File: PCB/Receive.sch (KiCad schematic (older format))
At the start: 36 parts, among them U18 MAX5394L, U19 MAX5394L, U20 MAX11116, U21 TLV3544, U22 MCP6L1

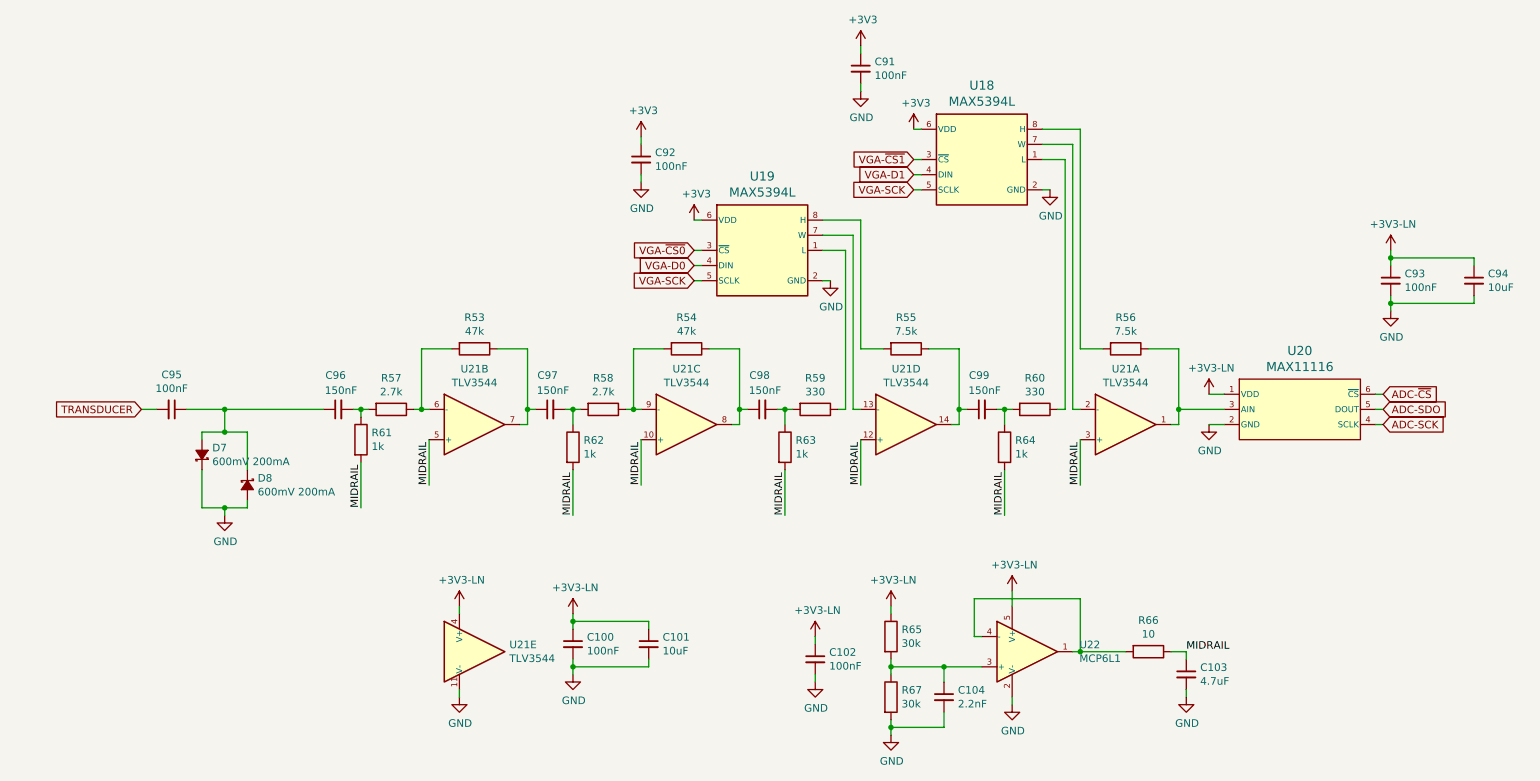
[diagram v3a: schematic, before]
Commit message: Remove unnecessary series resistors, rearrange connections on FPGA and microcontroller, rearrange debug pins, layout most of FPGA and microcontroller sections
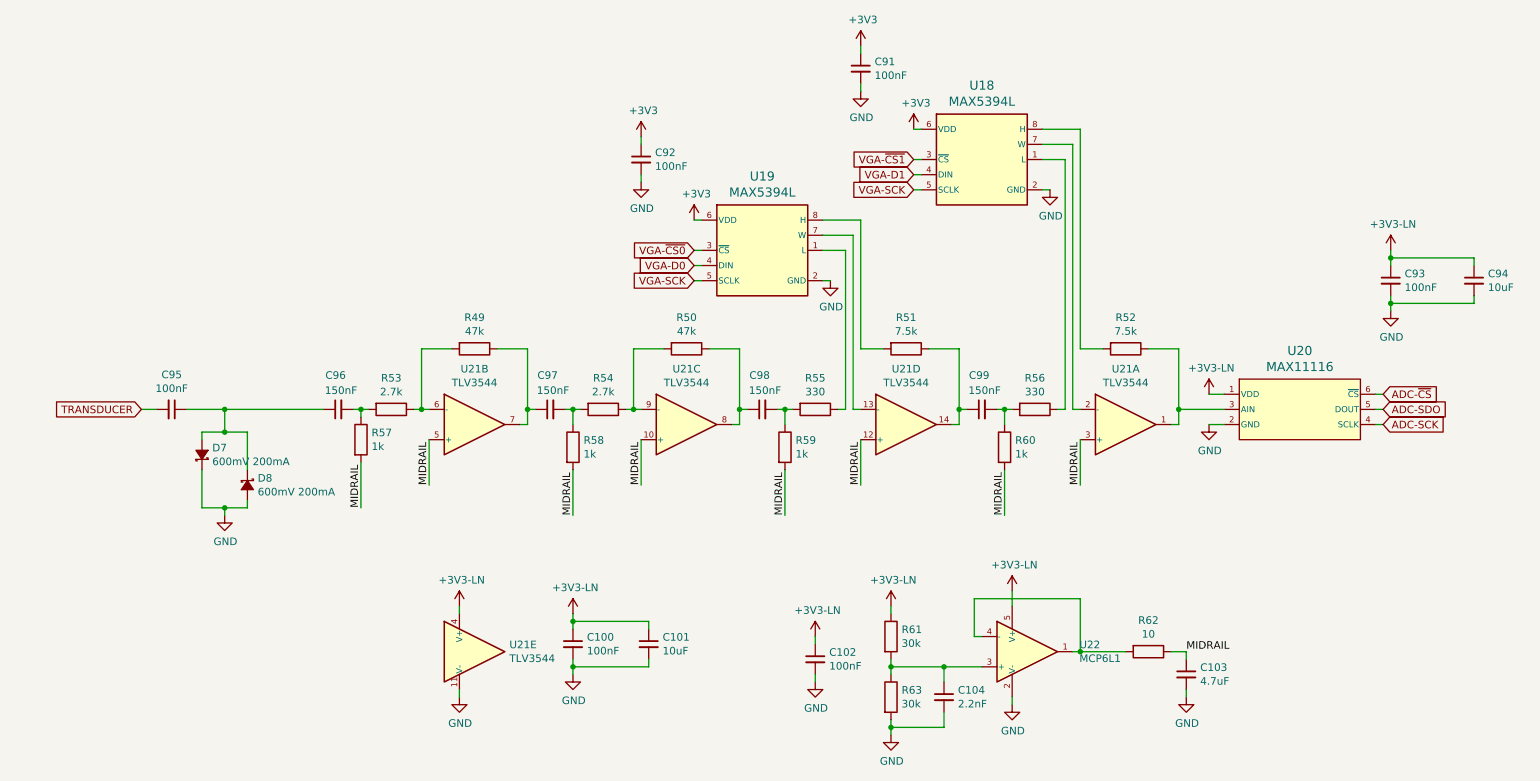
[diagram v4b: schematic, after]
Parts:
- renumbered R53 to R49, R54 to R50, R55 to R51, R56 to R52, R57 to R53, R58 to R54, R59 to R55, R60 to R56, R61 to R57, R62 to R58, R63 to R59, R64 to R60, R65 to R61, R66 to R62, R67 to R63

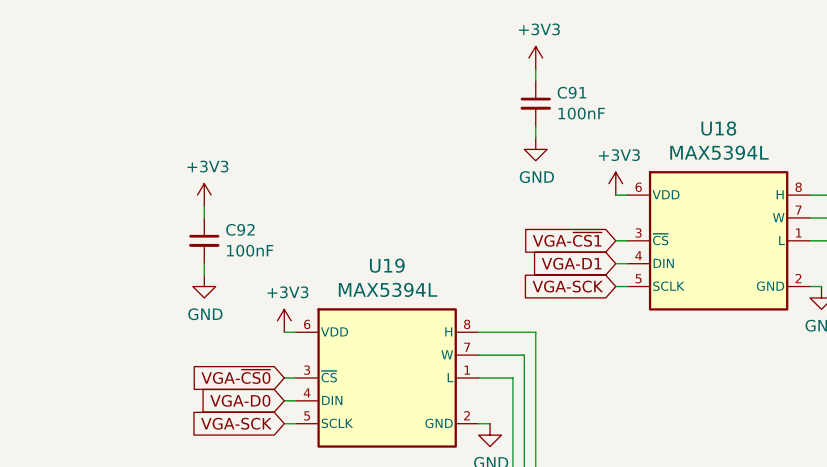
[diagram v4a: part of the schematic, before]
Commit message: Add additional mounting holes, optimize receive power supply connections for layout, simplify FPGA analog ground, layout 3v3 and 1v2 supplies
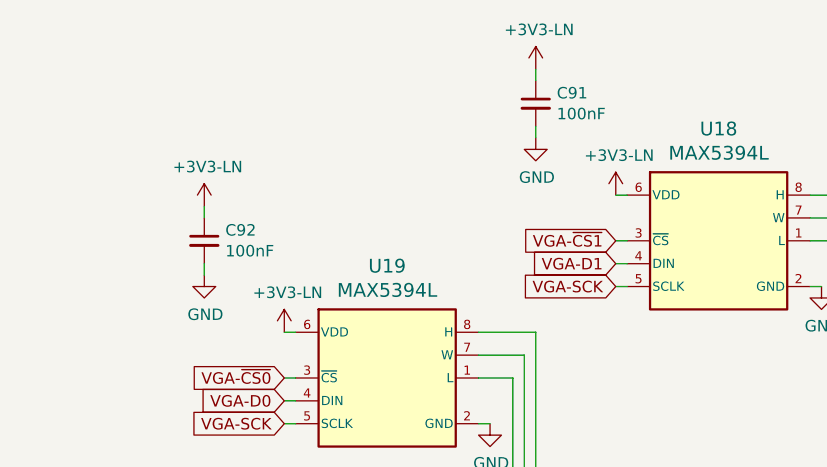
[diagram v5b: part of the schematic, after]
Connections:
- net +3V3 is gone; now on net +3V3-LN: C91.1, C92.1, U18.6 (VDD), U19.6 (VDD)
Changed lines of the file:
@@
 $EndComp
 $Comp
-L power:GND #PWR0164
+L power:GND #PWR0163
 U 1 1 5DE6B0BA
 P 8650 3850
-F 0 "#PWR0164" H 8650 3600 50  0001 C CNN
+F 0 "#PWR0163" H 8650 3600 50  0001 C CNN
 F 1 "GND" H 8655 3677 50  0000 C CNN
 F 2 "" H 8650 3850 50  0001 C CNN
@@
 	9750 3850 9800 3850
 $Comp
-L power:GND #PWR0165
+L power:GND #PWR0164
 U 1 1 5DE74334
 P 2150 4450
-F 0 "#PWR0165" H 2150 4200 50  0001 C CNN
+F 0 "#PWR0164" H 2150 4200 50  0001 C CNN
 F 1 "GND" H 2155 4277 50  0000 C CNN
 F 2 "" H 2150 4450 50  0001 C CNN
@@
 $EndComp
 $Comp
-L power:GND #PWR0162
+L power:GND #PWR0161
 U 1 1 5E3D4BAC
 P 9850 3100
-F 0 "#PWR0162" H 9850 2850 50  0001 C CNN
+F 0 "#PWR0161" H 9850 2850 50  0001 C CNN
 F 1 "GND" H 9855 2927 50  0000 C CNN
 F 2 "" H 9850 3100 50  0001 C CNN
@@
 	2150 3750 2800 3750
 $Comp
-L power:GND #PWR0172
+L power:GND #PWR0171
 U 1 1 5DF502DD
 P 6050 5550
-F 0 "#PWR0172" H 6050 5300 50  0001 C CNN
+F 0 "#PWR0171" H 6050 5300 50  0001 C CNN
 F 1 "GND" H 6055 5377 50  0000 C CNN
 F 2 "" H 6050 5550 50  0001 C CNN
@@
 	6050 5500 6050 5550
 $Comp
-L power:GND #PWR0171
+L power:GND #PWR0170
 U 1 1 5DF53278
 P 4450 5500
-F 0 "#PWR0171" H 4450 5250 50  0001 C CNN
+F 0 "#PWR0170" H 4450 5250 50  0001 C CNN
 F 1 "GND" H 4455 5327 50  0000 C CNN
 F 2 "" H 4450 5500 50  0001 C CNN
@@
 	4450 5450 4450 5500
 $Comp
-L power:GND #PWR0173
+L power:GND #PWR0172
 U 1 1 5DF58B7E
 P 3700 5650
-F 0 "#PWR0173" H 3700 5400 50  0001 C CNN
+F 0 "#PWR0172" H 3700 5400 50  0001 C CNN
 F 1 "GND" H 3705 5477 50  0000 C CNN
 F 2 "" H 3700 5650 50  0001 C CNN
@@
 	6350 3350 6500 3350
 $Comp
-L power:GND #PWR0161
+L power:GND #PWR0160
 U 1 1 5DFD250D
 P 6150 2900
-F 0 "#PWR0161" H 6150 2650 50  0001 C CNN
+F 0 "#PWR0160" H 6150 2650 50  0001 C CNN
 F 1 "GND" H 6155 2727 50  0000 C CNN
 F 2 "" H 6150 2900 50  0001 C CNN
@@
 	7700 2100 7700 3750
 $Comp
-L power:GND #PWR0158
+L power:GND #PWR0157
 U 1 1 5E02E9B9
 P 7600 2300
-F 0 "#PWR0158" H 7600 2050 50  0001 C CNN
+F 0 "#PWR0157" H 7600 2050 50  0001 C CNN
 F 1 "GND" H 7605 2127 50  0000 C CNN
 F 2 "" H 7600 2300 50  0001 C CNN
@@
 	7350 4950 7350 5050
 $Comp
-L power:GND #PWR0175
+L power:GND #PWR0174
 U 1 1 5E055C0B
 P 7350 5700
-F 0 "#PWR0175" H 7350 5450 50  0001 C CNN
+F 0 "#PWR0174" H 7350 5450 50  0001 C CNN
 F 1 "GND" H 7355 5527 50  0000 C CNN
 F 2 "" H 7350 5700 50  0001 C CNN
@@
 	6550 5050 6550 5100
 $Comp
-L power:GND #PWR0176
+L power:GND #PWR0175
 U 1 1 5E0AC1BB
 P 6550 5900
-F 0 "#PWR0176" H 6550 5650 50  0001 C CNN
+F 0 "#PWR0175" H 6550 5650 50  0001 C CNN
 F 1 "GND" H 6555 5727 50  0000 C CNN
 F 2 "" H 6550 5900 50  0001 C CNN
@@
 $EndComp
 $Comp
-L power:GND #PWR0174
+L power:GND #PWR0173
 U 1 1 5E0F1B62
 P 8500 5650
-F 0 "#PWR0174" H 8500 5400 50  0001 C CNN
+F 0 "#PWR0173" H 8500 5400 50  0001 C CNN
 F 1 "GND" H 8505 5477 50  0000 C CNN
 F 2 "" H 8500 5650 50  0001 C CNN
@@
 	6350 2500 6350 3350
 $Comp
-L power:GND #PWR0157
+L power:GND #PWR0156
 U 1 1 5E15077B
 P 4900 2250
-F 0 "#PWR0157" H 4900 2000 50  0001 C CNN
+F 0 "#PWR0156" H 4900 2000 50  0001 C CNN
 F 1 "GND" H 4905 2077 50  0000 C CNN
 F 2 "" H 4900 2250 50  0001 C CNN
@@
 	4900 1950 4900 2000
 $Comp
-L power:GND #PWR0154
+L power:GND #PWR0153
 U 1 1 5E168AE1
 P 6350 1650
-F 0 "#PWR0154" H 6350 1400 50  0001 C CNN
+F 0 "#PWR0153" H 6350 1400 50  0001 C CNN
 F 1 "GND" H 6355 1477 50  0000 C CNN
 F 2 "" H 6350 1650 50  0001 C CNN
@@
 	5250 2900 5300 2900
 $Comp
-L power:+3V3 #PWR0155
-U 1 1 5E033FD3
-P 6700 1900
-F 0 "#PWR0155" H 6700 1750 50  0001 C CNN
-F 1 "+3V3" H 6715 2073 50  0000 C CNN
-F 2 "" H 6700 1900 50  0001 C CNN
-F 3 "" H 6700 1900 50  0001 C CNN
-	1    6700 1900
-	1    0    0    -1
-$EndComp
-$Comp
-L power:+3V3 #PWR0153
-U 1 1 5E168AD7
-P 6350 1350
-F 0 "#PWR0153" H 6350 1200 50  0001 C CNN
-F 1 "+3V3" H 6365 1523 50  0000 C CNN
-F 2 "" H 6350 1350 50  0001 C CNN
-F 3 "" H 6350 1350 50  0001 C CNN
-	1    6350 1350
-	1    0    0    -1
-$EndComp
-$Comp
-L power:+3V3 #PWR0159
-U 1 1 5DFD98EC
-P 5250 2500
-F 0 "#PWR0159" H 5250 2350 50  0001 C CNN
-F 1 "+3V3" H 5265 2673 50  0000 C CNN
-F 2 "" H 5250 2500 50  0001 C CNN
-F 3 "" H 5250 2500 50  0001 C CNN
-	1    5250 2500
-	1    0    0    -1
-$EndComp
-$Comp
-L power:+3V3 #PWR0156
-U 1 1 5E150771
-P 4900 1950
-F 0 "#PWR0156" H 4900 1800 50  0001 C CNN
-F 1 "+3V3" H 4915 2123 50  0000 C CNN
-F 2 "" H 4900 1950 50  0001 C CNN
-F 3 "" H 4900 1950 50  0001 C CNN
-	1    4900 1950
-	1    0    0    -1
-$EndComp
-$Comp
-L Parts:+3V3-LN #PWR0163
+L Parts:+3V3-LN #PWR0162
 U 1 1 5E2A82B0
 P 8650 3650
-F 0 "#PWR0163" H 8650 3500 50  0001 C CNN
+F 0 "#PWR0162" H 8650 3500 50  0001 C CNN
 F 1 "+3V3-LN" H 8665 3823 50  0000 C CNN
 F 2 "" H 8650 3650 50  0001 C CNN
@@
 $EndComp
 $Comp
-L Parts:+3V3-LN #PWR0168
+L Parts:+3V3-LN #PWR0167
 U 1 1 5E2AAEEA
 P 6550 5050
-F 0 "#PWR0168" H 6550 4900 50  0001 C CNN
+F 0 "#PWR0167" H 6550 4900 50  0001 C CNN
 F 1 "+3V3-LN" H 6565 5223 50  0000 C CNN
 F 2 "" H 6550 5050 50  0001 C CNN
@@
 $EndComp
 $Comp
-L Parts:+3V3-LN #PWR0160
+L Parts:+3V3-LN #PWR0159
 U 1 1 5E2AD2A7
 P 9850 2700
-F 0 "#PWR0160" H 9850 2550 50  0001 C CNN
+F 0 "#PWR0159" H 9850 2550 50  0001 C CNN
 F 1 "+3V3-LN" H 9865 2873 50  0000 C CNN
 F 2 "" H 9850 2700 50  0001 C CNN
@@
 $EndComp
 $Comp
-L Parts:+3V3-LN #PWR0166
+L Parts:+3V3-LN #PWR0165
 U 1 1 5E2AFA32
 P 7350 4950
-F 0 "#PWR0166" H 7350 4800 50  0001 C CNN
+F 0 "#PWR0165" H 7350 4800 50  0001 C CNN
 F 1 "+3V3-LN" H 7365 5123 50  0000 C CNN
 F 2 "" H 7350 4950 50  0001 C CNN
@@
 $EndComp
 $Comp
-L Parts:+3V3-LN #PWR0170
+L Parts:+3V3-LN #PWR0169
 U 1 1 5E2AFFB8
 P 6050 5250
-F 0 "#PWR0170" H 6050 5100 50  0001 C CNN
+F 0 "#PWR0169" H 6050 5100 50  0001 C CNN
 F 1 "+3V3-LN" H 6065 5423 50  0000 C CNN
 F 2 "" H 6050 5250 50  0001 C CNN
@@
 $EndComp
 $Comp
-L Parts:+3V3-LN #PWR0169
+L Parts:+3V3-LN #PWR0168
 U 1 1 5E2B0647
 P 4450 5100
-F 0 "#PWR0169" H 4450 4950 50  0001 C CNN
+F 0 "#PWR0168" H 4450 4950 50  0001 C CNN
 F 1 "+3V3-LN" H 4465 5273 50  0000 C CNN
 F 2 "" H 4450 5100 50  0001 C CNN
@@
 $EndComp
 $Comp
-L Parts:+3V3-LN #PWR0167
+L Parts:+3V3-LN #PWR0166
 U 1 1 5E2B0FA3
 P 3700 5050
-F 0 "#PWR0167" H 3700 4900 50  0001 C CNN
+F 0 "#PWR0166" H 3700 4900 50  0001 C CNN
 F 1 "+3V3-LN" H 3715 5223 50  0000 C CNN
 F 2 "" H 3700 5050 50  0001 C CNN
@@
 	1    0    0    -1
 $EndComp
+$Comp
+L Parts:+3V3-LN #PWR0152
+U 1 1 5E5EAB30
+P 6350 1350
+F 0 "#PWR0152" H 6350 1200 50  0001 C CNN
+F 1 "+3V3-LN" H 6365 1523 50  0000 C CNN
+F 2 "" H 6350 1350 50  0001 C CNN
+F 3 "" H 6350 1350 50  0001 C CNN
+	1    6350 1350
+	1    0    0    -1
+$EndComp
+$Comp
+L Parts:+3V3-LN #PWR0154
+U 1 1 5E5EAF8D
+P 6700 1900
+F 0 "#PWR0154" H 6700 1750 50  0001 C CNN
+F 1 "+3V3-LN" H 6715 2073 50  0000 C CNN
+F 2 "" H 6700 1900 50  0001 C CNN
+F 3 "" H 6700 1900 50  0001 C CNN
+	1    6700 1900
+	1    0    0    -1
+$EndComp
+$Comp
+L Parts:+3V3-LN #PWR0158
+U 1 1 5E5EB373
+P 5250 2500
+F 0 "#PWR0158" H 5250 2350 50  0001 C CNN
+F 1 "+3V3-LN" H 5265 2673 50  0000 C CNN
+F 2 "" H 5250 2500 50  0001 C CNN
+F 3 "" H 5250 2500 50  0001 C CNN
+	1    5250 2500
+	1    0    0    -1
+$EndComp
+$Comp
+L Parts:+3V3-LN #PWR0155
+U 1 1 5E5EB9CD
+P 4900 1950
+F 0 "#PWR0155" H 4900 1800 50  0001 C CNN
+F 1 "+3V3-LN" H 4915 2123 50  0000 C CNN
+F 2 "" H 4900 1950 50  0001 C CNN
+F 3 "" H 4900 1950 50  0001 C CNN
+	1    4900 1950
+	1    0    0    -1
+$EndComp

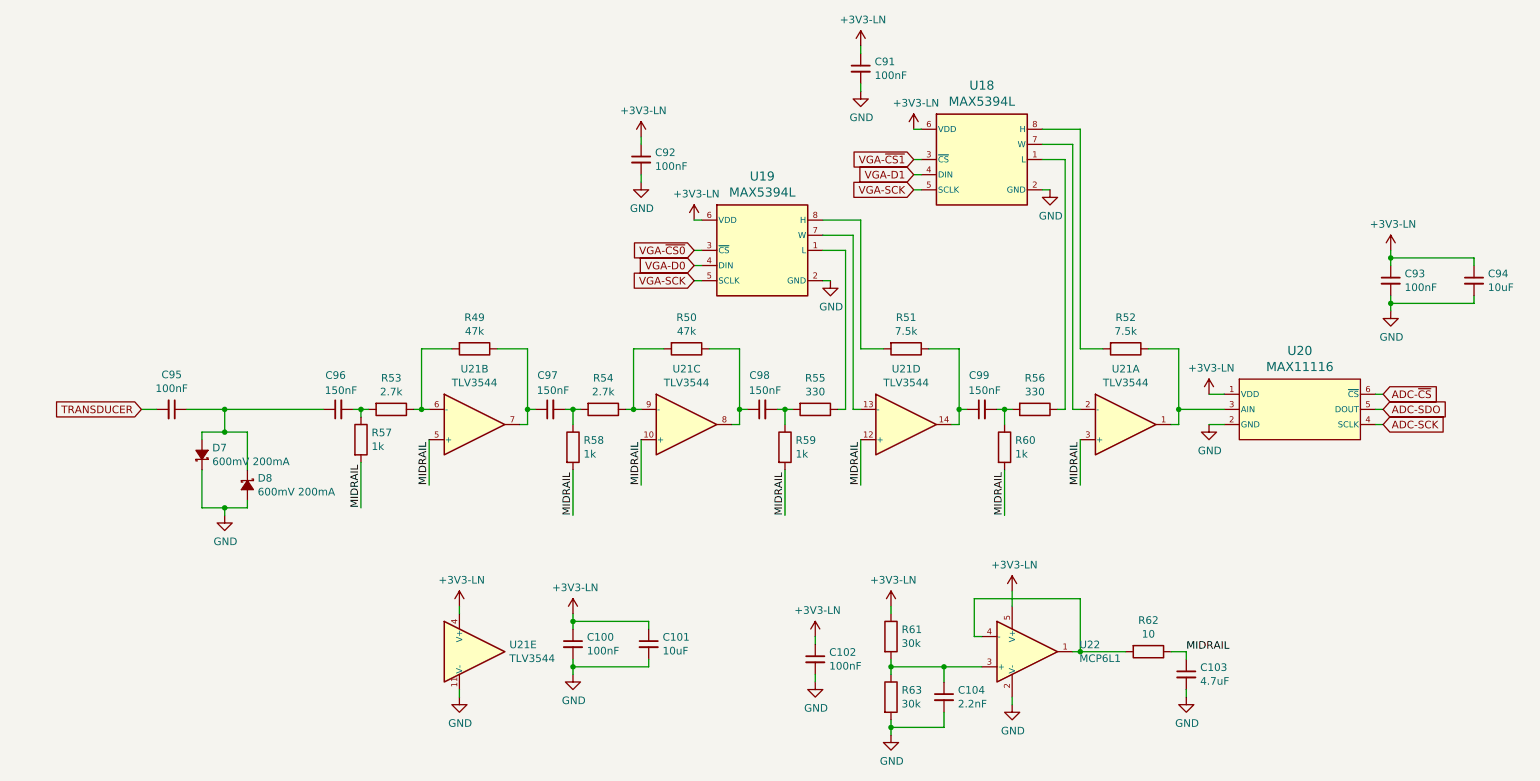
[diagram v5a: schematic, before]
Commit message: Adjust receive circuit to increase stability (hopefully less likely to oscillate)
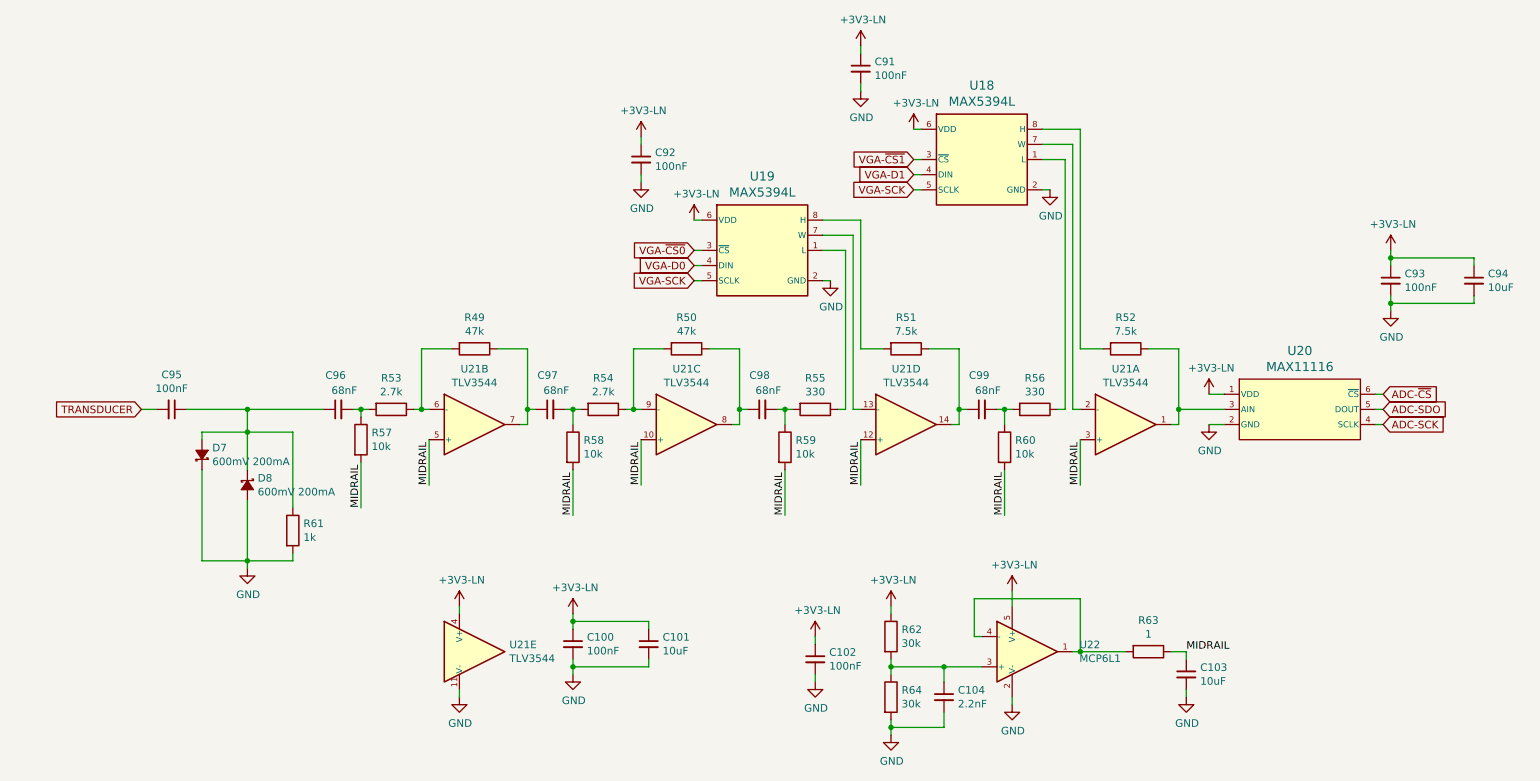
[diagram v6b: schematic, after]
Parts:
- added R61: 1k, Resistors_SMD:R_0603_HandSoldering, symbol Device:R
- C103: value 4.7uF -> 10uF; footprint Capacitors_SMD:C_0603_HandSoldering -> Capacitors_SMD:C_0805_HandSoldering
- C96, C97, C98, C99: value 150nF -> 68nF; footprint Capacitors_SMD:C_0603_HandSoldering -> Capacitors_SMD:C_0805_HandSoldering
- R57, R58, R59, R60: value 1k -> 10k
- R63: renamed from R62; value 10 -> 1
- renumbered R61 to R62, R63 to R64
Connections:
- net GND: now also R61.2
- net at C95.1, C96.1, D7.2 (A)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: now also R61.1

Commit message: Move 2.7k receive resistor to the correct location
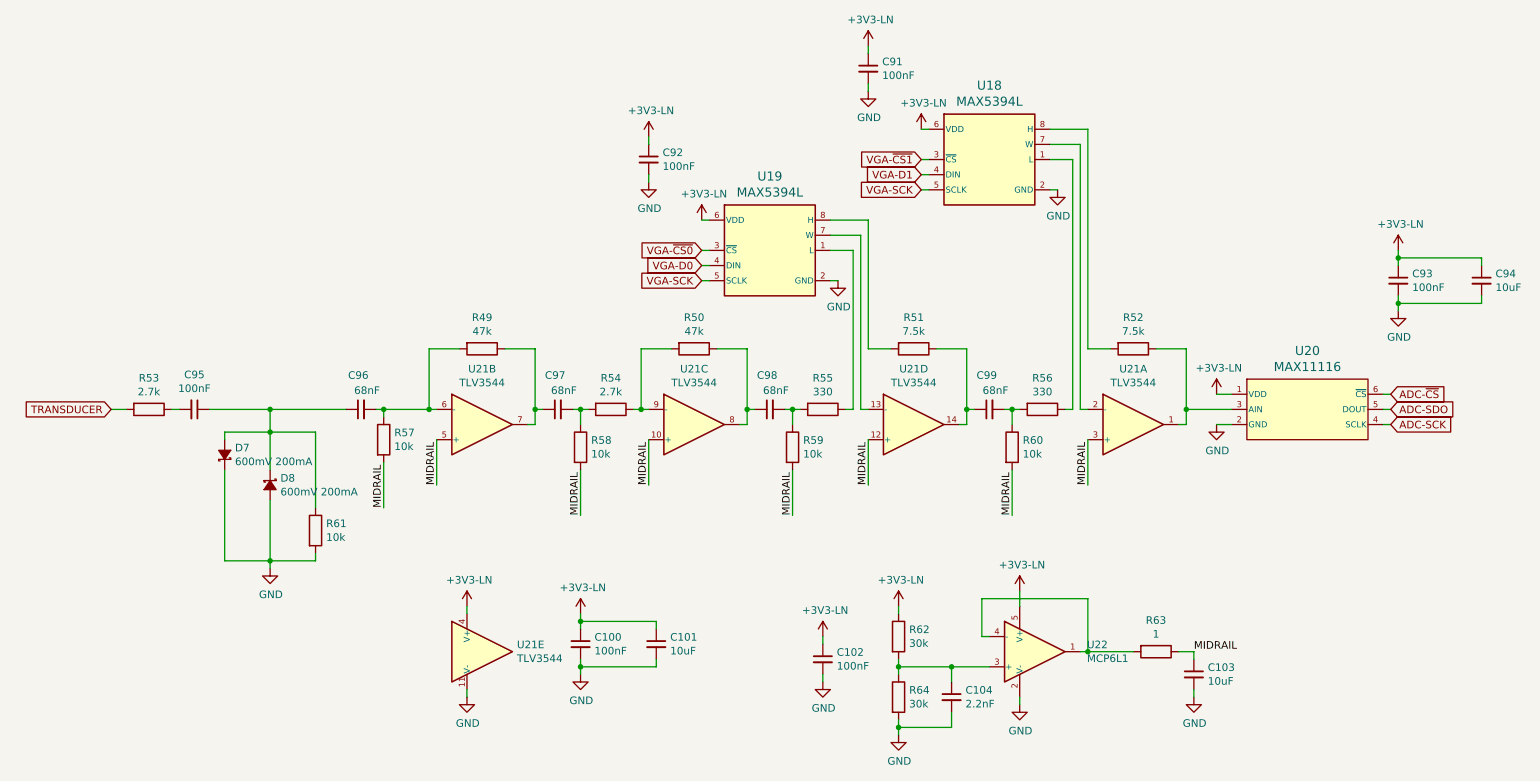
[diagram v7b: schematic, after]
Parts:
- R61: value 1k -> 10k
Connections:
- net TRANSDUCER: now also R53.2; no longer C95.2
- net at R49.2, U21.6 (-): now also C96.2, R57.1; no longer R53.1
- new net: C95.2, R53.1
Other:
- moved on the sheet: C100, C101, C102, C103, C104, C91, C92, C93, C94, C95, C96, C97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
